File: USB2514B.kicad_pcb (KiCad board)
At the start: 4 copper layers, 70 x 88 mm, 80 parts, among them J1 USB_A, J2 USB_C_Receptacle_USB2.0_16P, J3 USB_A, J4 USB_A, J6 USB_A, U1 USB2514B_Bi, U10 USBLC6-2P6, U11 USBLC6-2P6, U2 USBLC6-2P6, U3 AP22615AWU, U4 MCP1703Ax-330xxTT, U5 AP22615AWU, U6 AP22615AWU, U7 AP22615AWU, U8 USBLC6-2P6, U9 USBLC6-2P6, X1 24MHz

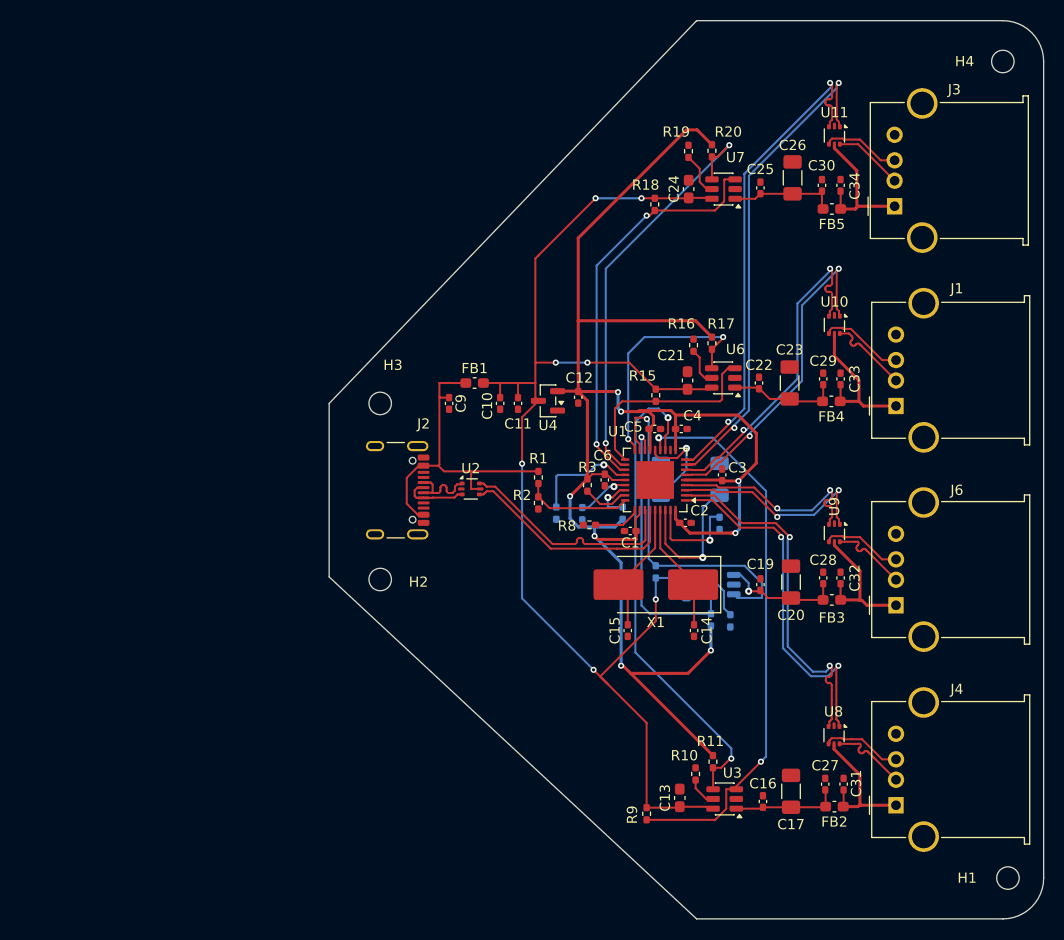
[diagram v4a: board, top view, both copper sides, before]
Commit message: Added connexion to 2 internal ground planes + some modifications on existing traces
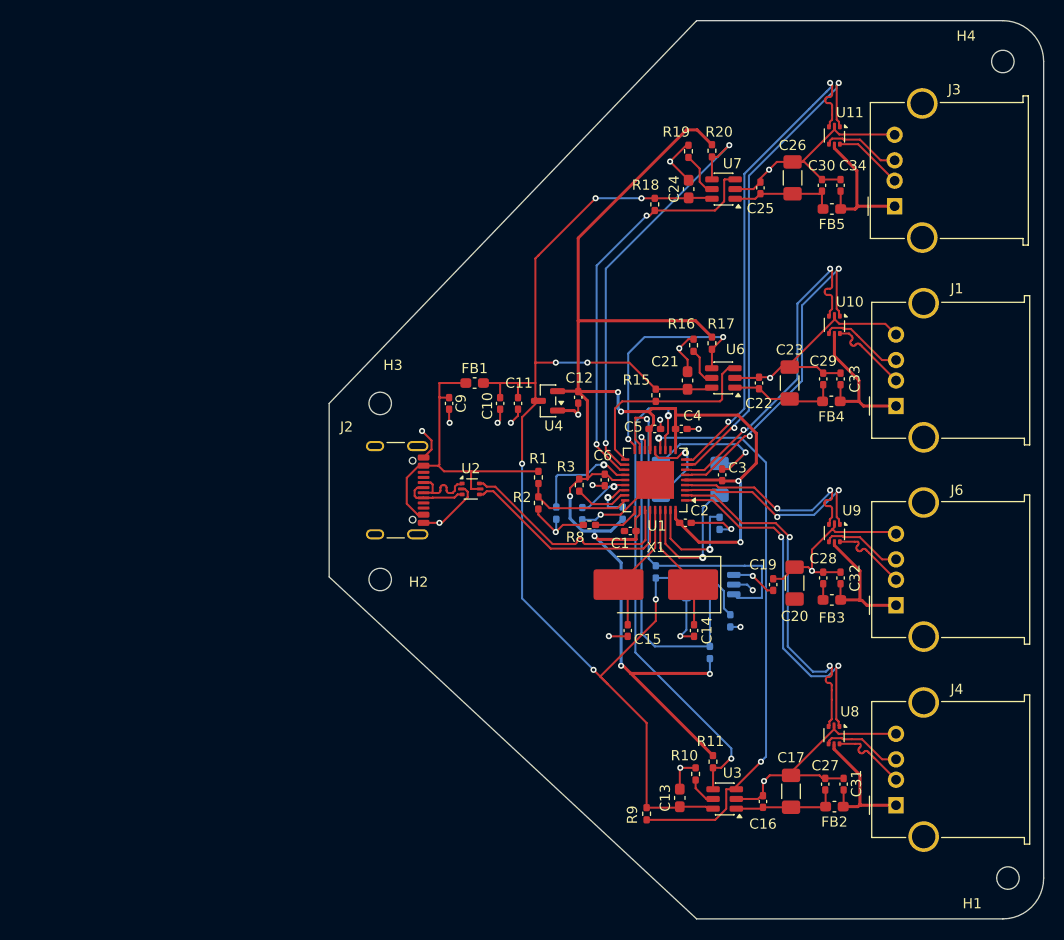
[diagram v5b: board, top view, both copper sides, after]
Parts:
- moved R14 3.20 mm to (157.3, 127.4)
- moved C19 1.25 mm to (163.5, 120.8)
- moved R3 0.80 mm to (144.5, 111.0)
- moved C20 0.36 mm to (165.6, 120.6)
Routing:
- net GND: track 0.00 -> 175.4 mm, vias 0 -> 24
- net /power switches1/EN: track 27.0 -> 33.0 mm
- net Net-(U5-OUT): track 11.9 -> 6.56 mm
- net /power switches/FAULT: track 55.5 -> 57.1 mm
- net Net-(U1-RBIAS): track 10.0 -> 11.3 mm
- net /power switches1/FAULT: track 34.7 -> 35.7 mm
- net Net-(U1-RESET_N): track 4.58 -> 5.38 mm
- net Net-(U1-CRFILT): track 9.70 -> 9.09 mm
- net /power switches/EN: track 48.6 -> 49.1 mm
- added copper zone on In1.Cu, net GND
- added copper zone on In2.Cu, net GND

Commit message: 1ere version module sans via de stitching
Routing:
- net GND: track 175.4 -> 176.8 mm, vias 24 -> 25
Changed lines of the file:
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@@
 		(tags "mountinghole M2")
 		(property "Reference" "H2"
-			(at 3.75 0.25 0)
+			(at 3.3 3.95 0)
 			(layer "F.SilkS")
 			(effects
@@
 	)
 	(segment
-		(start 147.5975 115.5)
-		(end 148.75 114.3475)
+		(start 160.3 116.6)
+		(end 160.3 110.8)
 		(width 0.3)
 		(layer "B.Cu")
@@
 	)
 	(segment
-		(start 160.3 116.6)
-		(end 160.3 110.8)
+		(start 147.1525 114.3475)
+		(end 148.75 114.3475)
 		(width 0.3)
 		(layer "B.Cu")
@@
 	)
 	(segment
-		(start 160.3 110.8)
-		(end 160.1 110.6)
+		(start 146 115.5)
+		(end 147.1525 114.3475)
 		(width 0.3)
 		(layer "B.Cu")
@@
 	)
 	(segment
-		(start 146 115.5)
-		(end 147.5975 115.5)
+		(start 160.3 110.8)
+		(end 160.1 110.6)
 		(width 0.3)
 		(layer "B.Cu")
@@
 	)
 	(segment
+		(start 148.9325 115.5)
+		(end 147.5 115.5)
+		(width 0.2)
+		(layer "F.Cu")
+		(net 2)
+	)
+	(segment
 		(start 163.8625 79.3375)
 		(end 163.1 80.1)
@@
 		(size 0.6)
 		(drill 0.3)
+		(layers "F.Cu" "B.Cu")
+		(net 2)
+	)
+	(via
+		(at 147.5 115.5)
+		(size 0.6)
+		(drill 0.3)

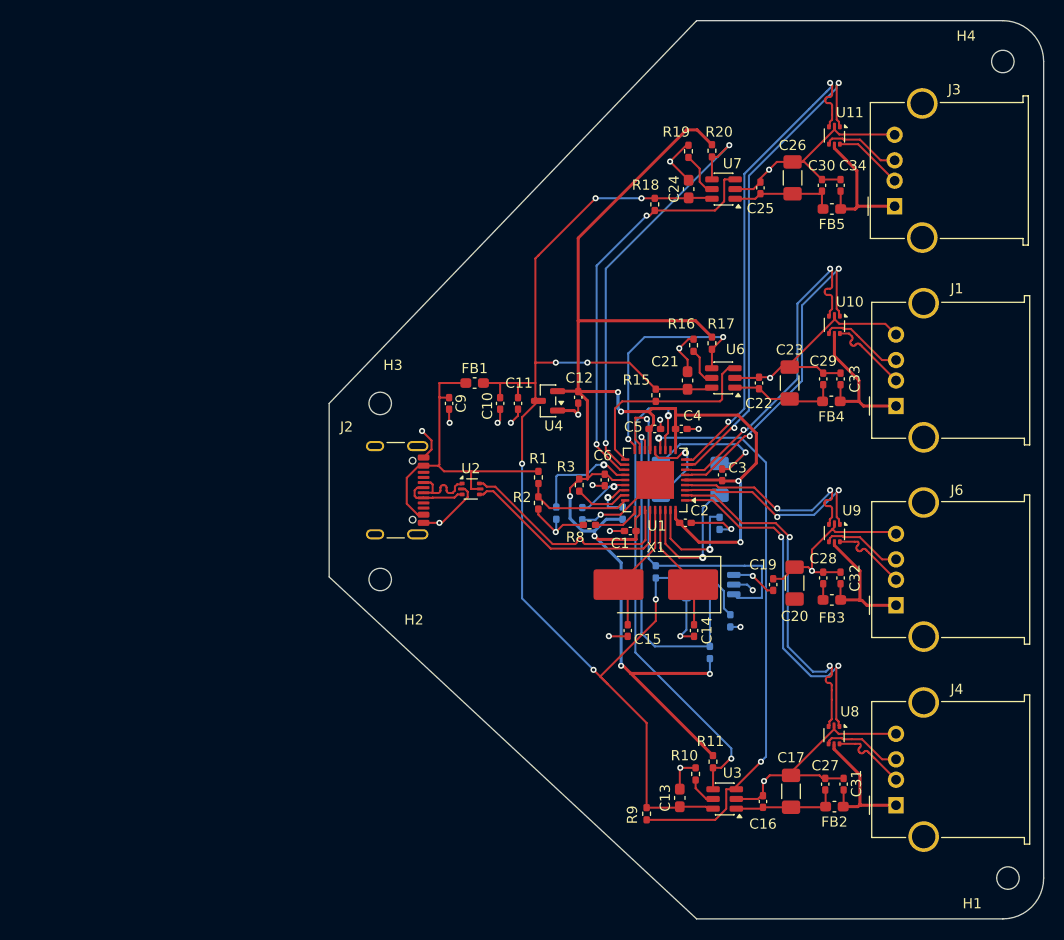
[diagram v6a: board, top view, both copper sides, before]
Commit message: Generate GBR files and add symbols information for JLC-PCB PCBA purchase
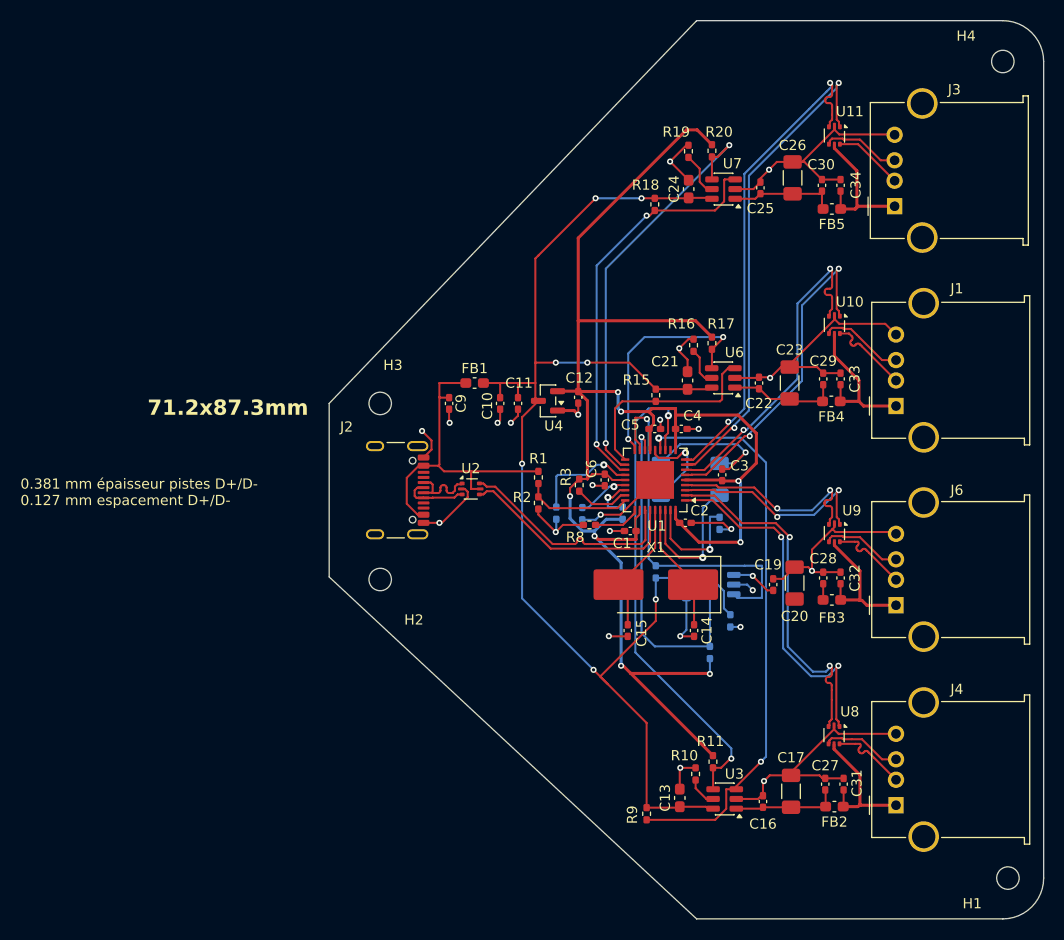
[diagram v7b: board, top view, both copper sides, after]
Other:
- board text added: "71.2x87.3mm"
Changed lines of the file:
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@@
 	(generator_version "9.0")
 	(general
-		(thickness 1.6)
+		(thickness 0.46)
 		(legacy_teardrops no)
 	)
@@
 			(layer "dielectric 2"
 				(type "core")
-				(thickness 1.24)
+				(thickness 0.1)
 				(material "FR4")
 				(epsilon_r 4.5)
@@
 			(outputformat 1)
 			(mirror no)
-			(drillshape 1)
+			(drillshape 0)
 			(scaleselection 1)
 			(outputdirectory "")
@@
 		(tags "SOT TO_SOT_SMD")
 		(property "Reference" "U6"
-			(at -1.1875 2.8 0)
+			(at -1.0875 2.5 0)
 			(layer "F.SilkS")
 			(effects
@@
 		(tags "capacitor handsolder")
 		(property "Reference" "C19"
-			(at 1.95 -1 0)
+			(at 1.95 -0.5 0)
 			(layer "F.SilkS")
 			(effects
@@
 		(tags "capacitor handsolder")
 		(property "Reference" "C15"
-			(at 0.85 -1.95 180)
+			(at 0.25 -1.35 270)
 			(layer "F.SilkS")
 			(effects
@@
 		(tags "SOT TO_SOT_SMD")
 		(property "Reference" "U3"
-			(at -0.75 2.55 0)
+			(at -0.95 2.45 0)
 			(layer "F.SilkS")
 			(effects
@@
 		(tags "capacitor handsolder")
 		(property "Reference" "C30"
-			(at 1.9325 -0.03 180)
+			(at 2.0325 -0.08 180)
 			(layer "F.SilkS")
 			(effects
@@
 		(tags "capacitor handsolder")
 		(property "Reference" "C6"
-			(at -2.4 0.2 180)
+			(at -1.1 1.3 270)
 			(layer "F.SilkS")
 			(effects
@@
 		(tags "SOT-666")
 		(property "Reference" "U11"
-			(at -2.25 -1.5 180)
+			(at -2.35 -1.5 180)
 			(layer "F.SilkS")
 			(effects
@@
 		(tags "capacitor handsolder")
 		(property "Reference" "C3"
-			(at 0.7 1.5 180)
+			(at 0.9 1.7 180)
 			(layer "F.SilkS")
 			(effects
@@
 		(tags "capacitor handsolder")
 		(property "Reference" "C34"
-			(at 1.9325 1.2 0)
+			(at 0.0325 1.5 90)
 			(layer "F.SilkS")
 			(effects
@@
 		(tags "capacitor handsolder")
 		(property "Reference" "C1"
-			(at 1 -1.2 0)
+			(at 0.8 -1.2 0)
 			(layer "F.SilkS")
 			(effects
@@
 		(tags "resistor handsolder")
 		(property "Reference" "R3"
-			(at -1.8 1.3 180)
+			(at -0.8 1.3 270)
 			(layer "F.SilkS")
 			(effects
@@
 		(tags "capacitor handsolder")
 		(property "Reference" "C31"
-			(at 0.0675 1.25 90)
+			(at 0.1 1.3 90)
 			(layer "F.SilkS")
 			(effects
@@
 		(tags "capacitor handsolder")
 		(property "Reference" "C5"
-			(at -2.1 -0.2 0)
+			(at -2.4 -0.4 0)
 			(layer "F.SilkS")
 			(effects
@@
 		(layer "Edge.Cuts")
 	)
+	(gr_text "71.2x87.3mm"
+		(at 102.2 104.3 0)
+		(layer "F.SilkS")
+		(effects
+			(font
+				(size 1.5 1.5)
+				(thickness 0.3)
+				(bold yes)
+			)
+			(justify left bottom)
+		)
+	)
 	(gr_text "0.381 mm épaisseur pistes D+/D-\n0.127 mm espacement D+/D-"
 		(at 89.75 113.082 0)
-		(layer "Edge.Cuts")
+		(layer "F.SilkS")
 		(effects
 			(font
